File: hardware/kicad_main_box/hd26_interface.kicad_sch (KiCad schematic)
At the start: 0 parts

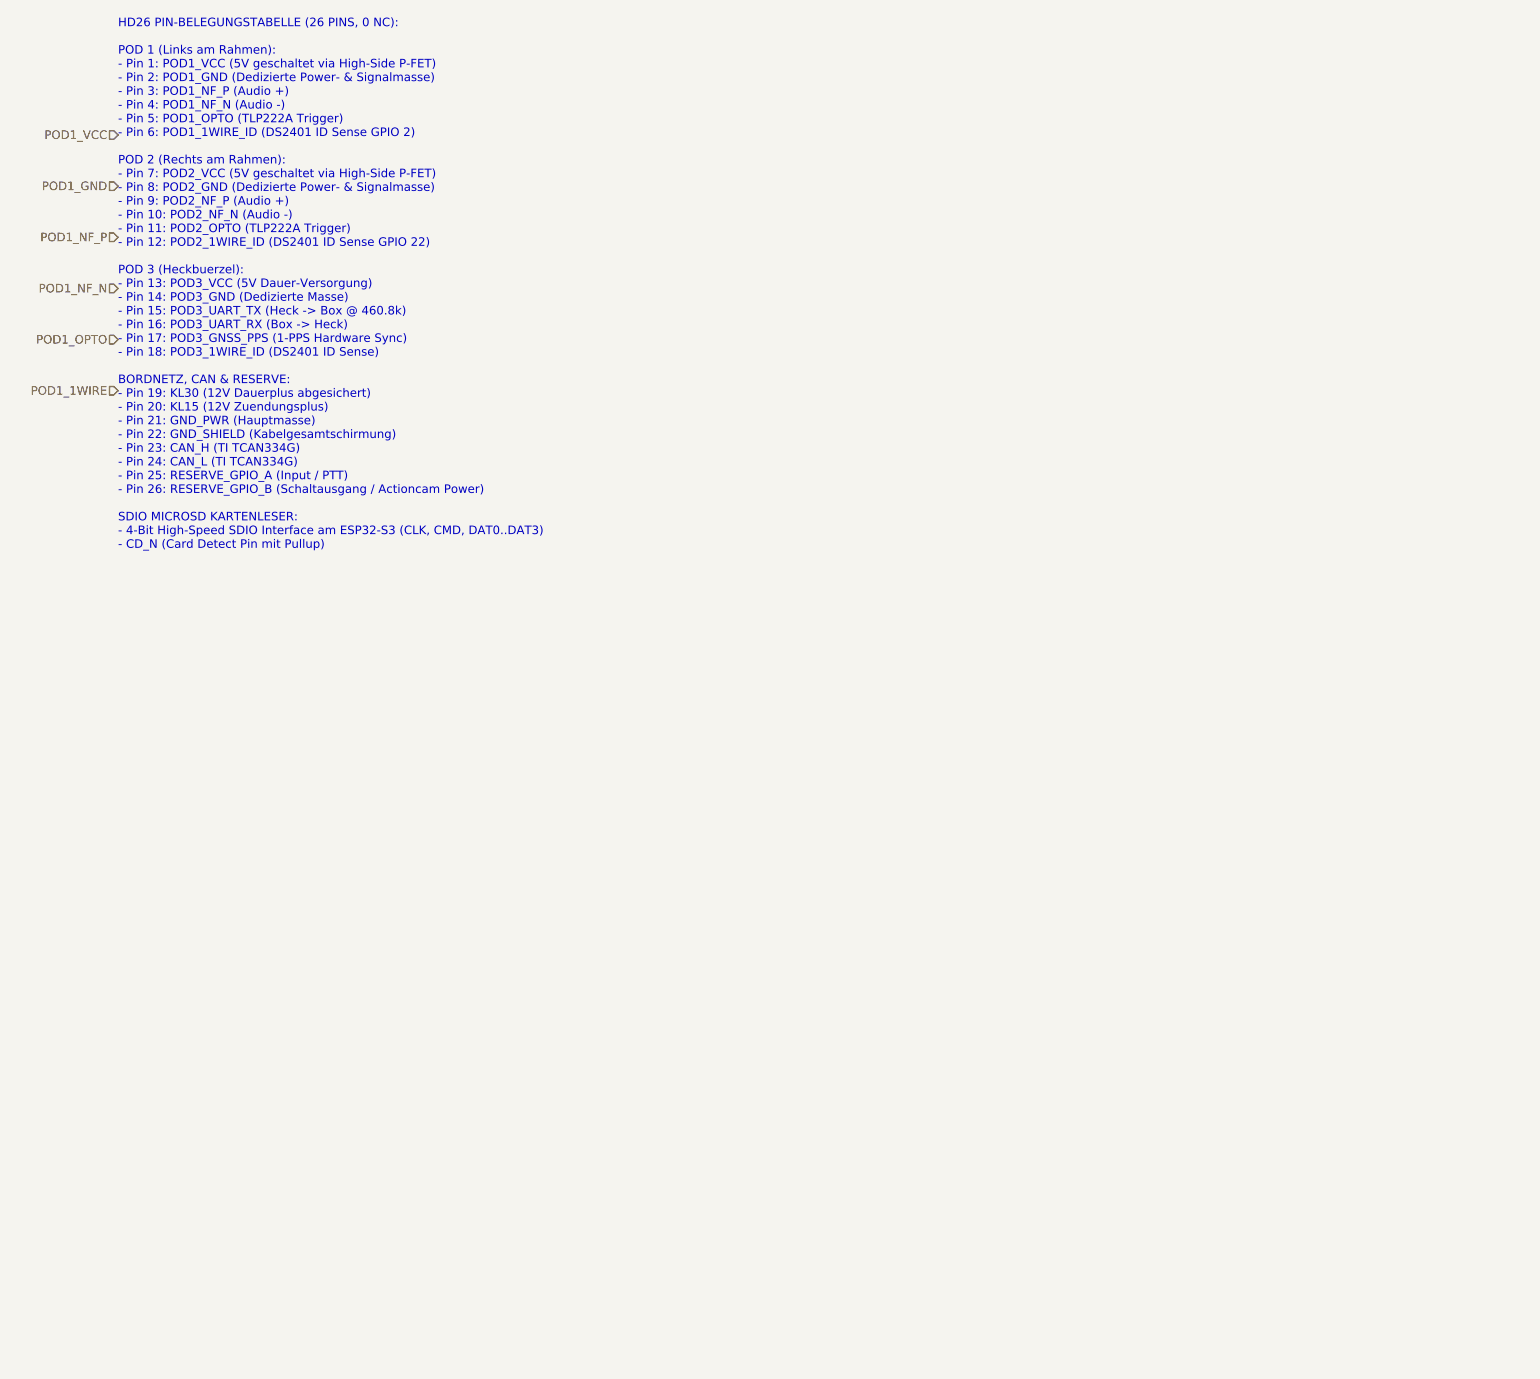
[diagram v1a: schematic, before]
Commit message: feat(kicad): Implement full graphical electronic schematic drawings (symbols, pins, wires, components) for all boards
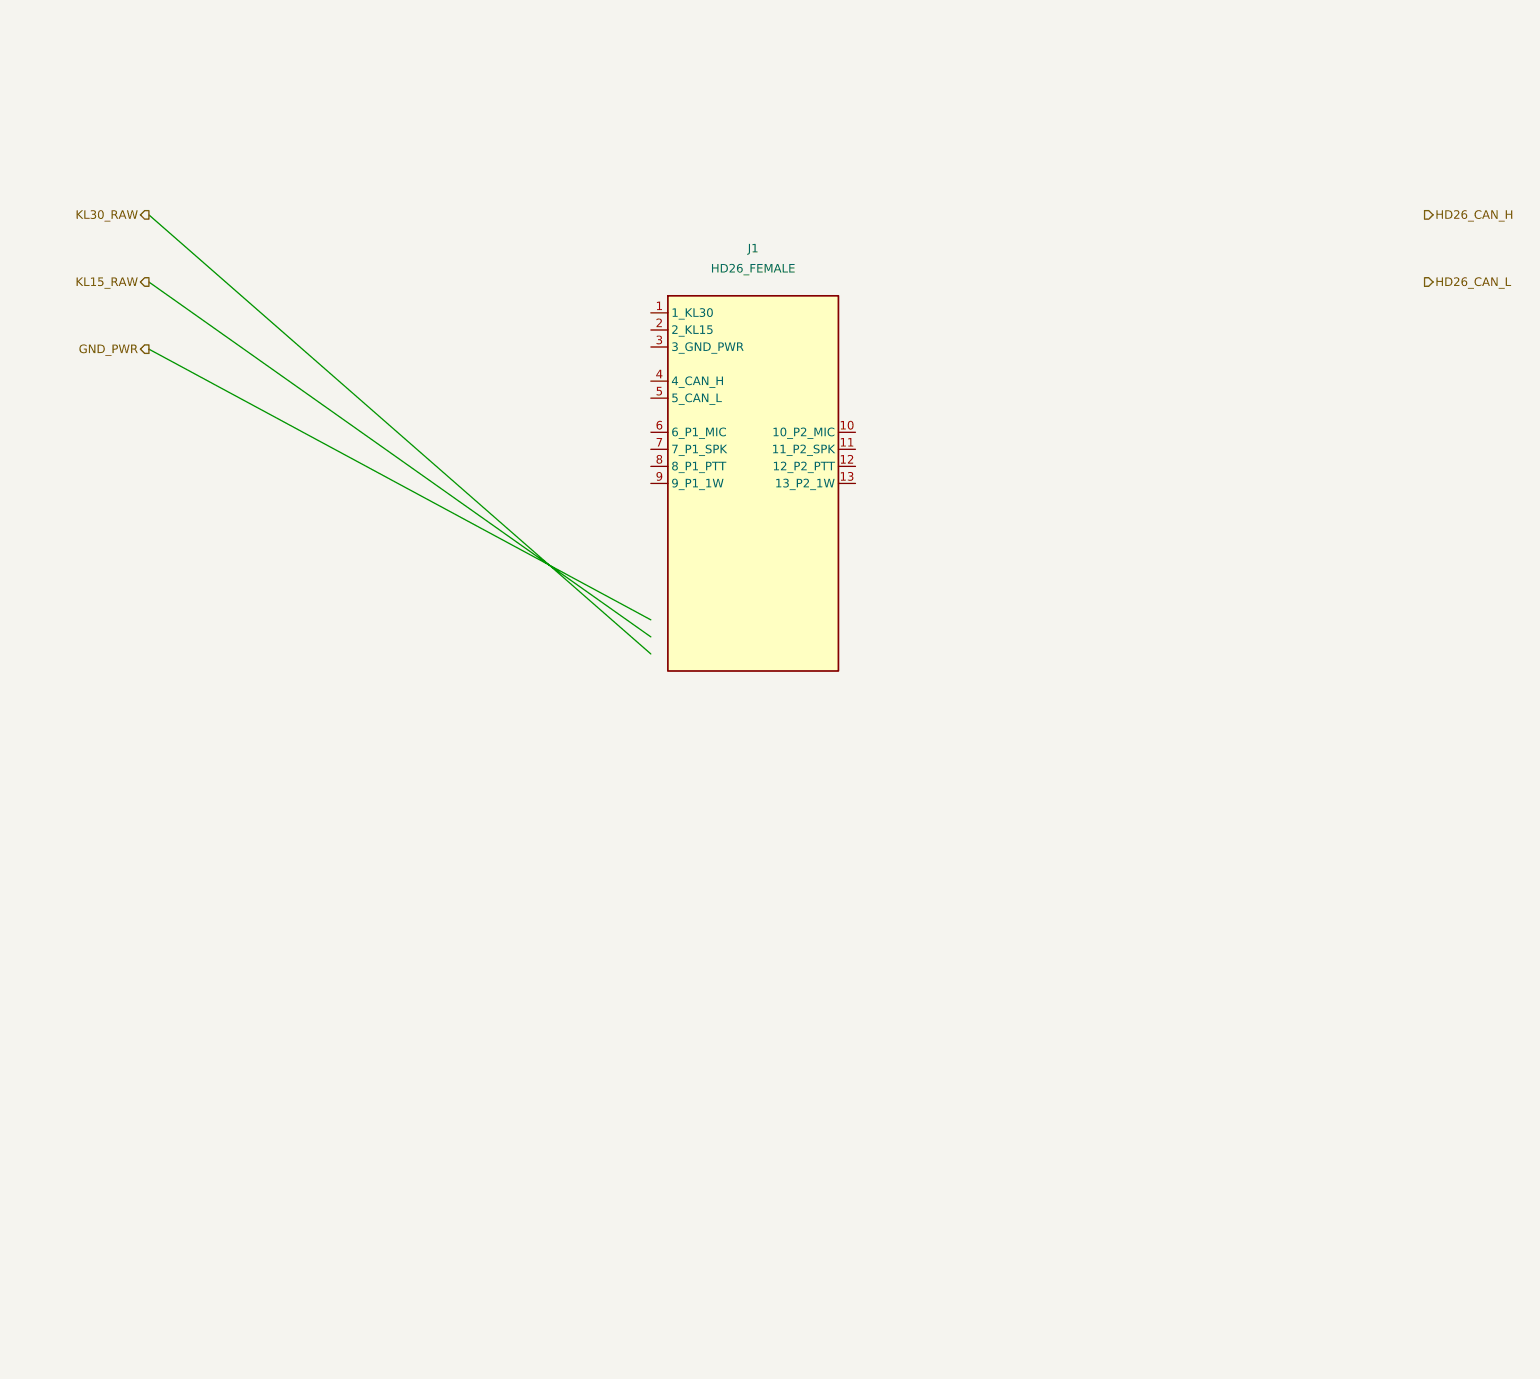
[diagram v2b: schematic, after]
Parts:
- added J1: HD26_FEMALE, symbol Connector:HD26_Female
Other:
- note removed: "HD26 PIN-BELEGUNGSTABELLE (26 PINS, 0 NC): POD 1 (Links am Rahmen): - Pin 1: POD1_VCC (5V geschaltet via High-Side P-FET) - Pin 2: POD1_GND (Dedizierte Power- & Signalmasse) - Pin 3: POD1_NF_P (Audio +) - Pin 4: POD1_NF_N (Audio -) - Pin 5: POD1_OPTO (TLP222A Trigger) - Pin 6: POD1_1WIRE_ID (DS2401 ID Sense GPIO 2) POD 2 (Rechts am Rahmen): - Pin 7: POD2_VCC (5V geschaltet via High-Side P-FET) - 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"
- company: (none) -> OpenMotorBridge Open Source Hardware
- title: OpenMotorBridge v8.0 - HD26 Flansch, 2x13 Header & SDIO Slot -> OpenMotorBridge v8.0 - HD26 Matrix-Schnittstelle & Bordnetz
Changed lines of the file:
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@@
-(kicad_sch (version 20260206) (generator "eeschema") (generator_version "10.0")
-  (paper "A3")
-  (title_block
-    (title "OpenMotorBridge v8.0 - HD26 Flansch, 2x13 Header & SDIO Slot")
-    (date "2026-08-23")
-    (rev "v8.0")
-    (comment 1 "CN1: HD26 Flanschbuchse IP67 <-> J1: 2x13 Pfostenverbinder")
-    (comment 2 "26 Pins, 0 NC - Symmetrisches 6-Ader Interface fuer Pod 1, Pod 2, Pod 3")
-  )
-  (hierarchical_label "POD1_VCC" (shape input) (at 25.4 38.1 180)
-    (effects (font (size 1.27 1.27)) (justify right))
-  )
-  (hierarchical_label "POD1_GND" (shape input) (at 25.4 45.72 180)
-    (effects (font (size 1.27 1.27)) (justify right))
-  )
-  (hierarchical_label "POD1_NF_P" (shape input) (at 25.4 53.34 180)
-    (effects (font (size 1.27 1.27)) (justify right))
-  )
-  (hierarchical_label "POD1_NF_N" (shape input) (at 25.4 60.96 180)
-    (effects (font (size 1.27 1.27)) (justify right))
-  )
-  (hierarchical_label "POD1_OPTO" (shape input) (at 25.4 68.58 180)
-    (effects (font (size 1.27 1.27)) (justify right))
-  )
-  (hierarchical_label "POD1_1WIRE" (shape input) (at 25.4 76.2 180)
-    (effects (font (size 1.27 1.27)) (justify right))
-  )
-  (text "HD26 PIN-BELEGUNGSTABELLE (26 PINS, 0 NC):\n\nPOD 1 (Links am Rahmen):\n- Pin 1: POD1_VCC (5V geschaltet via High-Side P-FET)\n- Pin 2: POD1_GND (Dedizierte Power- & Signalmasse)\n- Pin 3: POD1_NF_P (Audio +)\n- Pin 4: POD1_NF_N (Audio -)\n- Pin 5: POD1_OPTO (TLP222A Trigger)\n- Pin 6: POD1_1WIRE_ID (DS2401 ID Sense GPIO 2)\n\nPOD 2 (Rechts am Rahmen):\n- Pin 7: POD2_VCC (5V geschaltet via High-Side P-FET)\n- Pin 8: POD2_GND (Dedizierte Power- & Signalmasse)\n- Pin 9: POD2_NF_P (Audio +)\n- Pin 10: POD2_NF_N (Audio -)\n- Pin 11: POD2_OPTO (TLP222A Trigger)\n- Pin 12: POD2_1WIRE_ID (DS2401 ID Sense GPIO 22)\n\nPOD 3 (Heckbuerzel):\n- Pin 13: POD3_VCC (5V Dauer-Versorgung)\n- Pin 14: POD3_GND (Dedizierte Masse)\n- Pin 15: POD3_UART_TX (Heck -> Box @ 460.8k)\n- Pin 16: POD3_UART_RX (Box -> Heck)\n- Pin 17: POD3_GNSS_PPS (1-PPS Hardware Sync)\n- Pin 18: POD3_1WIRE_ID (DS2401 ID Sense)\n\nBORDNETZ, CAN & RESERVE:\n- Pin 19: KL30 (12V Dauerplus abgesichert)\n- Pin 20: KL15 (12V Zuendungsplus)\n- Pin 21: GND_PWR (Hauptmasse)\n- Pin 22: GND_SHIELD (Kabelgesamtschirmung)\n- Pin 23: CAN_H (TI TCAN334G)\n- Pin 24: CAN_L (TI TCAN334G)\n- Pin 25: RESERVE_GPIO_A (Input / PTT)\n- Pin 26: RESERVE_GPIO_B (Schaltausgang / Actioncam Power)\n\nSDIO MICROSD KARTENLESER:\n- 4-Bit High-Speed SDIO Interface am ESP32-S3 (CLK, CMD, DAT0..DAT3)\n- CD_N (Card Detect Pin mit Pullup)" (at 25.4 100.0 0)
-    (effects (font (size 1.27 1.27)) (justify left bottom))
-  )
+(kicad_sch
+	(version 20260206)
+	(generator "eeschema")
+	(generator_version "10.0")
+	(paper "A3")
+	(title_block
+		(title "OpenMotorBridge v8.0 - HD26 Matrix-Schnittstelle & Bordnetz")
+		(date "2026-08-24")
+		(rev "v8.0")
+		(company "OpenMotorBridge Open Source Hardware")
+		(comment 1 "HD26 High-Density 26-Pin Industriesteckverbinder fuer alle externen Leitungen")
+		(comment 2 "Port 1 (Fahrer), Port 2 (Sozius), Port 3 (M8 Heck), KL30/KL15, CAN-Bus, Garmin Line-In")
+	)
+	;; =========================================================================
+	;; Hierarchical Labels
+	;; =========================================================================
+	(hierarchical_label "KL30_RAW" (shape output) (at 30.0 50.0 180) (effects (font (size 1.27 1.27)) (justify right)))
+	(hierarchical_label "KL15_RAW" (shape output) (at 30.0 60.0 180) (effects (font (size 1.27 1.27)) (justify right)))
+	(hierarchical_label "GND_PWR" (shape output) (at 30.0 70.0 180) (effects (font (size 1.27 1.27)) (justify right)))
+	(hierarchical_label "HD26_CAN_H" (shape output) (at 220.0 50.0 0) (effects (font (size 1.27 1.27)) (justify left)))
+	(hierarchical_label "HD26_CAN_L" (shape output) (at 220.0 60.0 0) (effects (font (size 1.27 1.27)) (justify left)))
+	;; =========================================================================
+	;; Symbols Placement
+	;; =========================================================================
+	;; J1: HD26 High Density Female D-Sub
+	(symbol (lib_id "Connector:HD26_Female") (at 120.0 90.0 0) (unit 1)
+		(in_bom yes) (on_board yes) (dnp no)
+		(property "Reference" "J1" (at 120.0 55.0 0) (effects (font (size 1.27 1.27))))
+		(property "Value" "HD26_FEMALE" (at 120.0 58.0 0) (effects (font (size 1.27 1.27))))
+		(pin "1")
+		(pin "2")
+		(pin "3")
+		(pin "4")
+		(pin "5")
+		(pin "6")
+		(pin "7")
+		(pin "8")
+		(pin "9")
+		(pin "10")
+		(pin "11")
+		(pin "12")
+		(pin "13")
+	)
+	;; Wires
+	(wire (pts (xy 30.0 50.0) (xy 104.76 115.4)) (stroke (width 0) (type solid)))
+	(wire (pts (xy 30.0 60.0) (xy 104.76 112.86)) (stroke (width 0) (type solid)))
+	(wire (pts (xy 30.0 70.0) (xy 104.76 110.32)) (stroke (width 0) (type solid)))
 )
